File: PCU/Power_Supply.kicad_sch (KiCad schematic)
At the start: 23 parts, among them IC6 BD433M5FP-CE2, J5 XT30PW-M

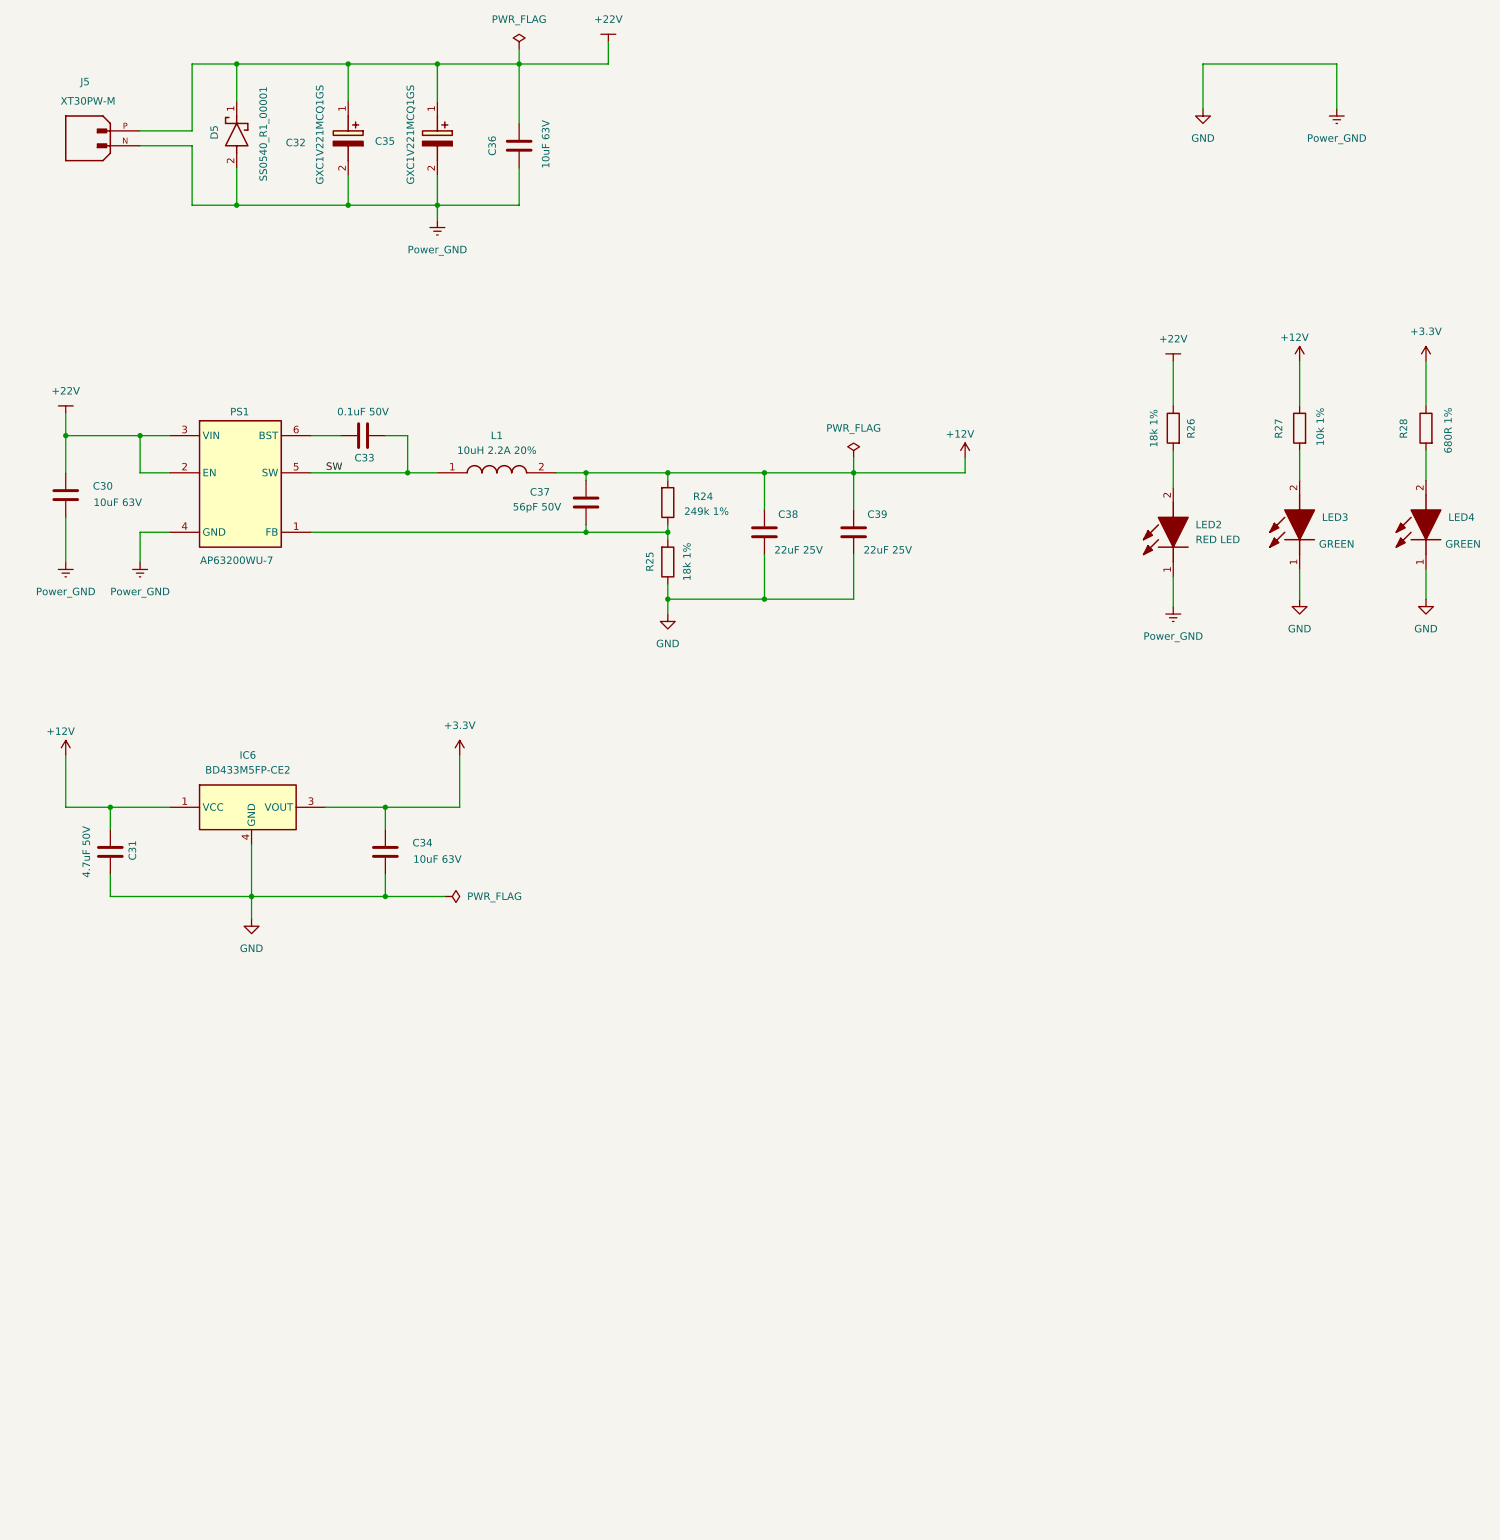
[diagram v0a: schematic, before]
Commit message: ESC Block Updated
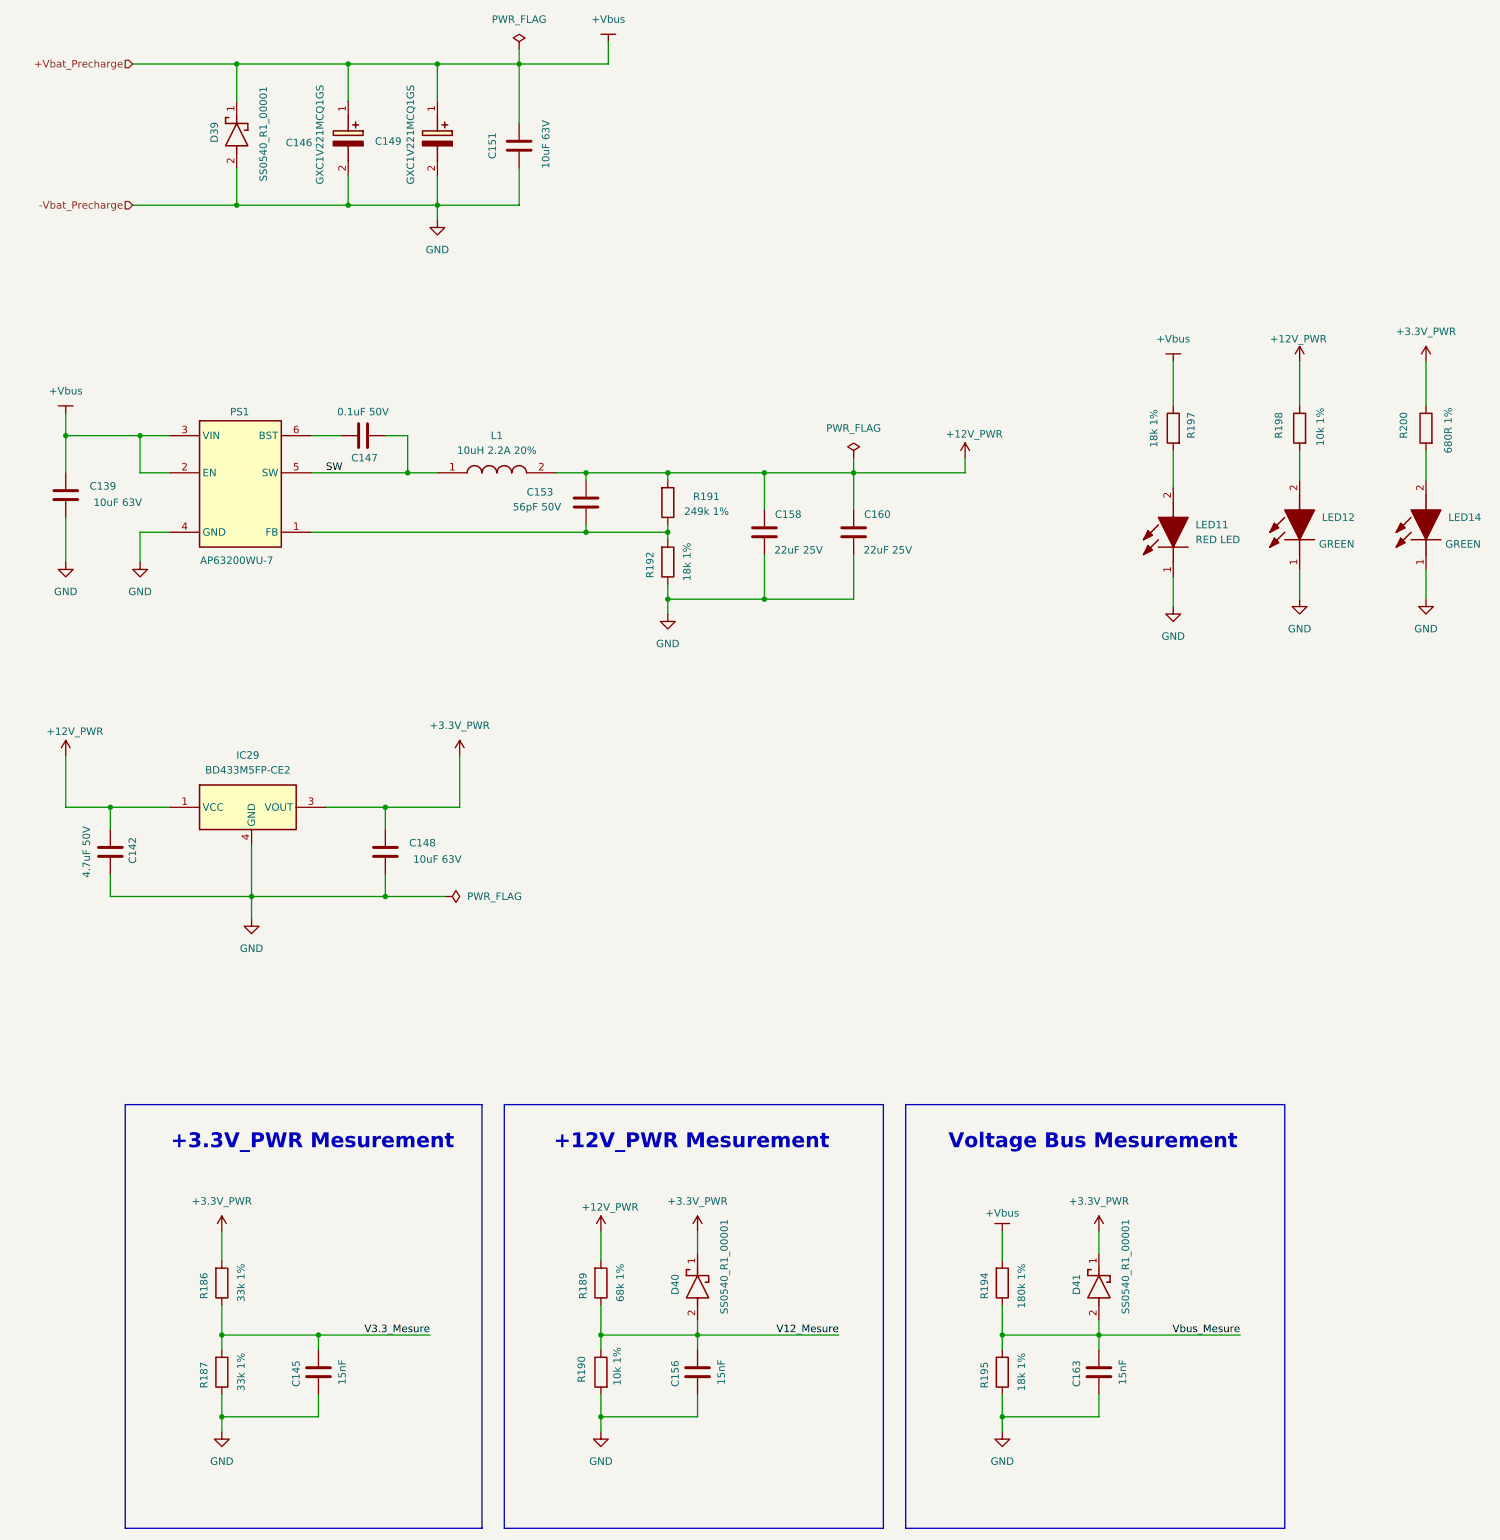
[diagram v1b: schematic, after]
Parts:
- removed J5: XT30PW-M, BassinaLib_Connectors:AMASS_XT30PW-M, symbol BassinaLib_Connectors:XT30PW-M
- added C145, C156, C163: 15nF, Capacitor_SMD:C_0603_1608Metric, symbol Device:C
- added D40, D41: SS0540_R1_00001, BassingaLib_Diodes:SOD3816X135N, symbol BassingaLib_Diodes:SS0540_R1_00001
- added R186, R187: 33k 1%, Resistor_SMD:R_0603_1608Metric, symbol Device:R
- added R189: 68k 1%, Resistor_SMD:R_0603_1608Metric, symbol Device:R
- added R190: 10k 1%, Resistor_SMD:R_0603_1608Metric, symbol Device:R
- added R194: 180k 1%, Resistor_SMD:R_0603_1608Metric, symbol Device:R
- added R195: 18k 1%, Resistor_SMD:R_0603_1608Metric, symbol Device:R
- renumbered C30 to C139, C31 to C142, C32 to C146, C33 to C147, C34 to C148, C35 to C149, C36 to C151, C37 to C153, C38 to C158, C39 to C160, D5 to D39, IC6 to IC29, LED2 to LED11, LED3 to LED12, LED4 to LED14, R24 to R191, R25 to R192, R26 to R197, R27 to R198, R28 to R200
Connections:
- net GND: now also C145.1, C156.1, C163.1, R187.1, R190.2, R195.1
- net +12V renamed +12V_PWR
- net +12V_PWR: now also R189.2
- net +22V renamed +Vbus
- net +Vbus: now also R194.2
- net +3.3V renamed +3.3V_PWR
- net +3.3V_PWR: now also D40.1 (K), D41.1 (K), R186.2
- new net V12_Mesure: C156.2, D40.2 (A), R189.1, R190.1
- new net V3.3_Mesure: C145.2, R186.1, R187.2
- new net Vbus_Mesure: C163.2, D41.2 (A), R194.1, R195.2
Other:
- note added: "+12V_PWR Mesurement"
- note added: "+3.3V_PWR Mesurement"
- note added: "Voltage Bus Mesurement"
